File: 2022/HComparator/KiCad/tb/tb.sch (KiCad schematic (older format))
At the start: 3 parts

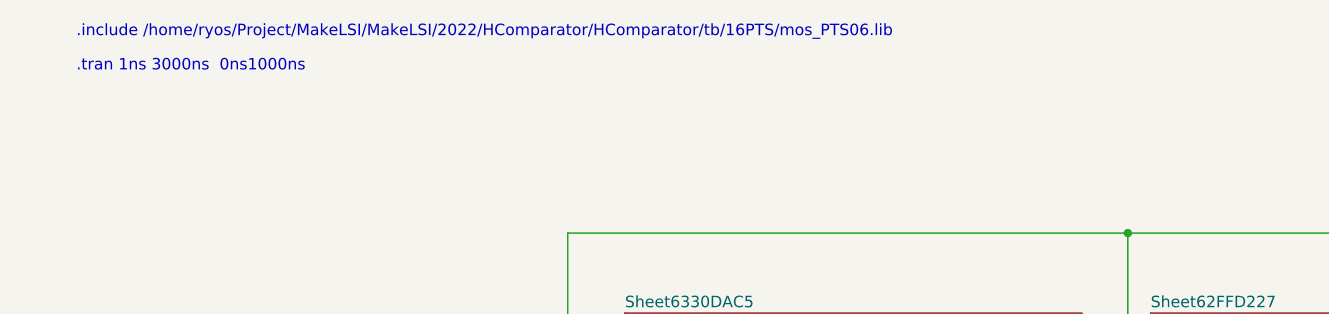
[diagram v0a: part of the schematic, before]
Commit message: テストベンチを通し、シミュレーション結果も得た。 さらに、再度 LVS を確認した。
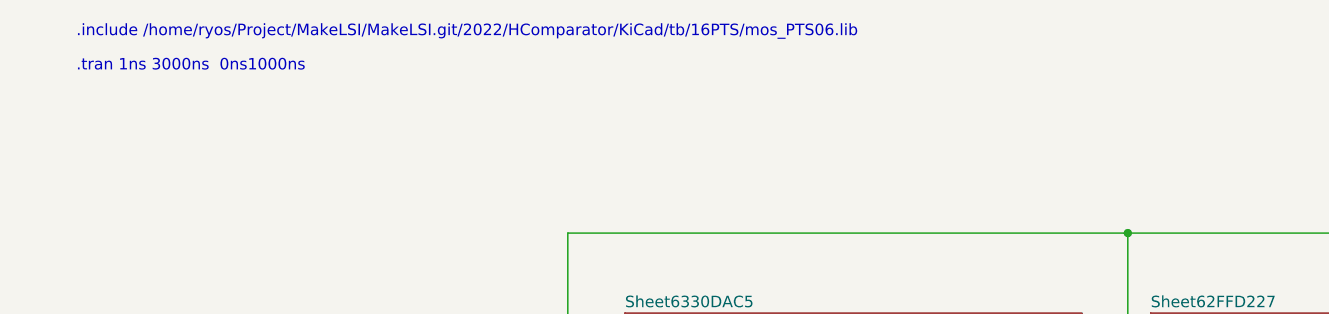
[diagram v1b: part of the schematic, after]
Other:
- note added: ".include /home/ryos/Project/MakeLSI/MakeLSI.git/2022/HComparator/KiCad/tb/16PTS/mos_PTS06.lib"
- note removed: ".include /home/ryos/Project/MakeLSI/MakeLSI/2022/HComparator/HComparator/tb/16PTS/mos_PTS06.lib"
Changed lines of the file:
@@
 	2550 4050 2550 3700
 Text Notes 2150 1800 0    50   ~ 0
-.include /home/ryos/Project/MakeLSI/MakeLSI/2022/HComparator/HComparator/tb/16PTS/mos_PTS06.lib
+.include /home/ryos/Project/MakeLSI/MakeLSI.git/2022/HComparator/KiCad/tb/16PTS/mos_PTS06.lib
 Text Notes 2150 1950 0    50   ~ 0
 .tran 1ns 3000ns  0ns1000ns
